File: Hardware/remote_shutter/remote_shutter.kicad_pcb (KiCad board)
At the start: 4 copper layers, 62.5 x 57 mm, 67 parts, among them J1 USB_C_Receptacle_USB2.0, J2 OLED, J3 AudioJack3, J4 Buzzer, J6 Switch, Q1 DMN2056U, Q2 DMN2056U, Q3 BC847BDW1, SW1 RotaryEncoder_Switch, U1 AZ1117-3.3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

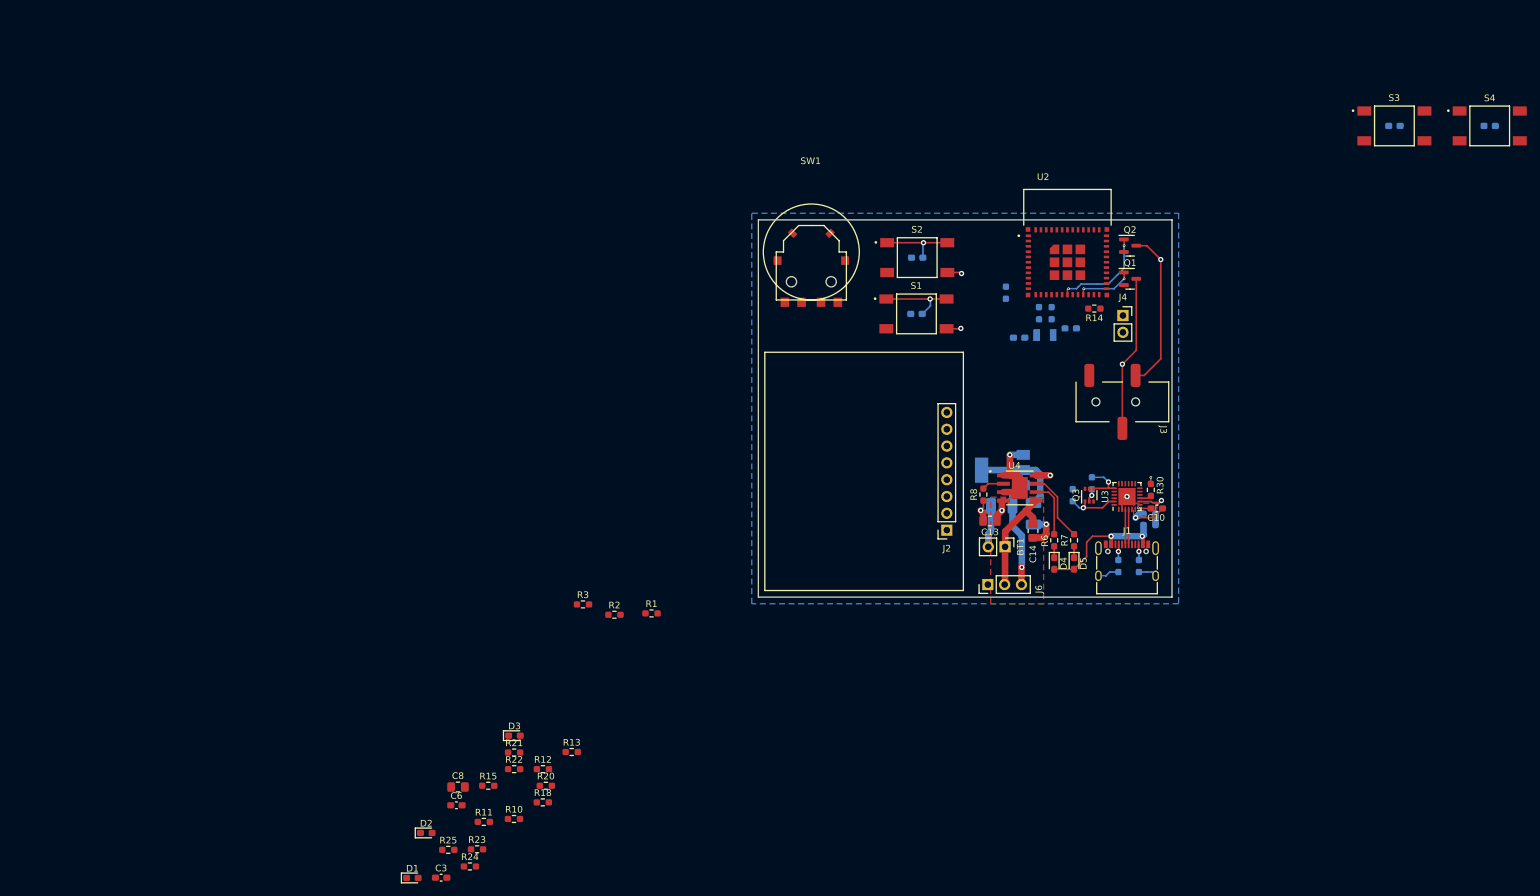
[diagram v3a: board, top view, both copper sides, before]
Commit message: Further routing. Fixed I2C net connection.
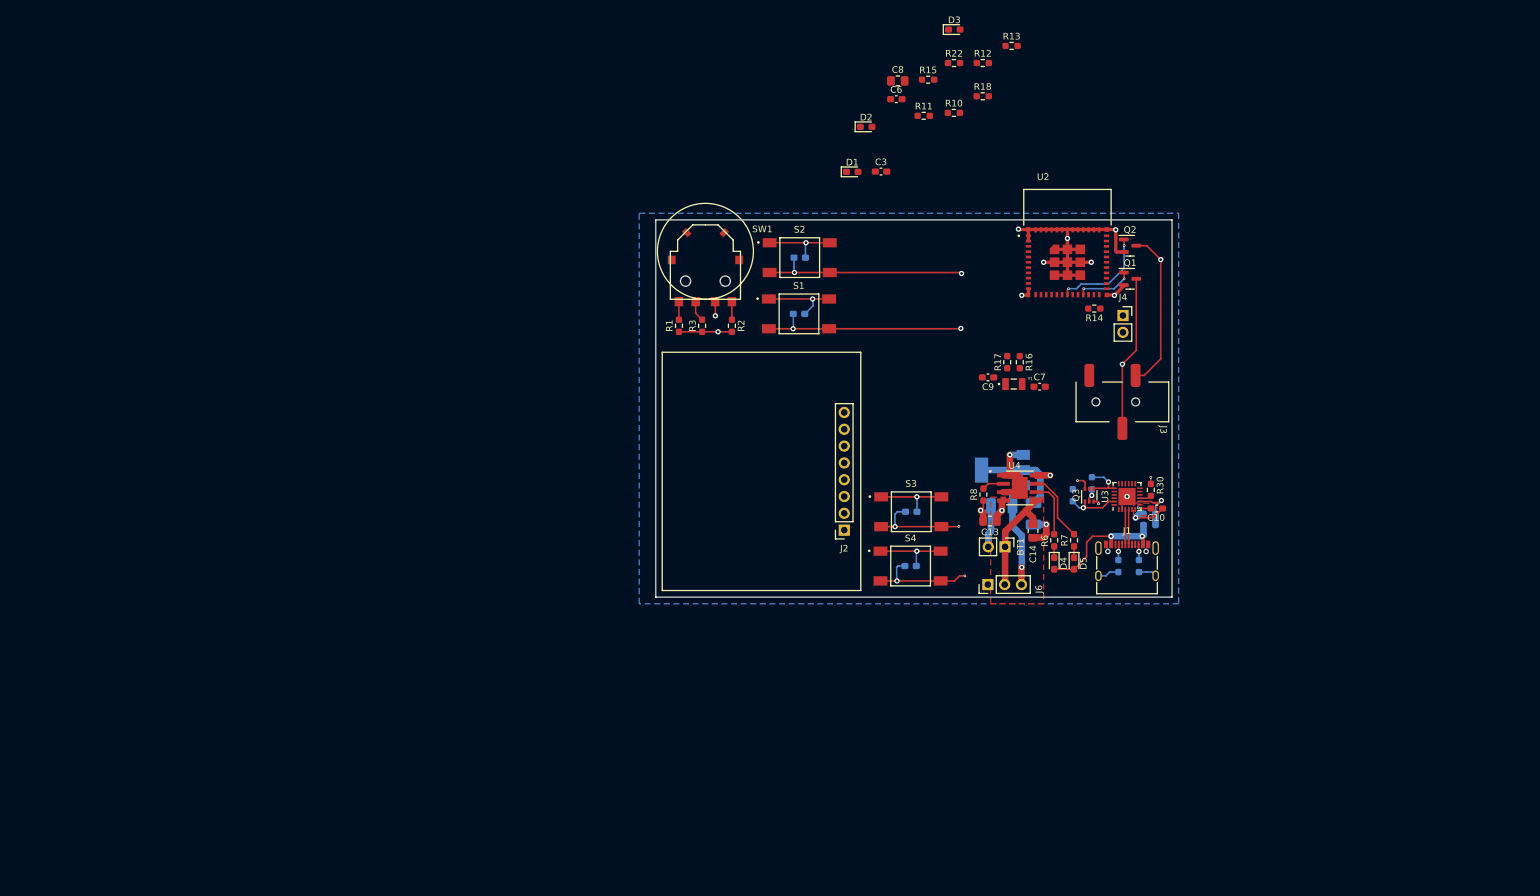
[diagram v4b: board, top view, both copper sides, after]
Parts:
- removed R19, R20, R21, R23, R24, R25: 10k, Resistor_SMD:R_0603_1608Metric_Pad0.98x0.95mm_HandSolder
- C7, C9, R16, R17, Y1: moved to F.Cu
- moved D1 125.7 mm to (170.7, 26.2)
- moved C6 125.7 mm to (177.3, 15.3)
- moved C8 125.7 mm to (177.6, 12.5)
- moved D2 125.7 mm to (172.8, 19.4)
- moved R10 125.7 mm to (186.0, 17.3)
- moved R11 125.7 mm to (181.5, 17.8)
- moved R12 125.7 mm to (190.4, 9.80)
- moved R15 125.7 mm to (182.2, 12.3)
- moved R18 125.7 mm to (190.4, 14.8)
- moved R22 125.7 mm to (186.1, 9.80)
- moved C3 125.7 mm to (175.0, 26.2)
- moved D3 125.7 mm to (186.1, 4.74)
- moved R13 125.7 mm to (194.8, 7.21)
- moved C5 109.9 mm to (179.5, 85.8)
- moved S4 109.9 mm to (179.5, 85.8)
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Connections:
- U2 pad 10: /MCU/B3 -> unconnected-(U2-Pad10)
- U2 pad 16: unconnected-(U2-Pad16) -> /MCU/A3
- U2 pad 27: /MCU/A3 -> unconnected-(U2-Pad27)
- U2 pad 28: /MCU/B3 -> unconnected-(U2-Pad28)
- U2 pad 4: /MCU/C3 -> unconnected-(U2-Pad4)
- U2 pad 9: /MCU/A3 -> unconnected-(U2-Pad9)
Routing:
- net GND: track 67.0 -> 140.0 mm, vias 7 -> 17
- net /MCU/EN: track 0.00 -> 43.2 mm, vias 0 -> 3
- net /MCU/IO0: track 0.00 -> 38.8 mm, vias 0 -> 3
- net /MCU/Interfaces/SHUTTER: track 61.5 -> 90.6 mm, vias 2 -> 3
- net /MCU/Interfaces/FOCUS: track 52.3 -> 81.4 mm, vias 2 -> 3
- net +3V3: track 16.8 -> 24.8 mm, vias 2 -> 3
- net /MCU/Interfaces/A2: track 0.00 -> 3.14 mm
- net /MCU/Interfaces/A1: track 0.00 -> 2.74 mm
- net /MCU/Interfaces/A0: track 0.00 -> 2.74 mm
- net Net-(C7-Pad1): track 0.57 -> 0.00 mm
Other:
- board size 62.5 x 57 mm -> 78 x 57 mm

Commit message: Initial routing complete
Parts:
- moved R18 71.6 mm to (165.3, 81.9)
- moved R22 71.6 mm to (165.3, 78.3)
- moved D3 43.7 mm to (181.1, 48.2)
- moved R15 41.8 mm to (204.0, 48.0), turned to -90 degrees
- moved R12 38.6 mm to (186.1, 48.2)
- moved R13 35.4 mm to (195.2, 42.6), turned to 90 degrees
- moved C8 28.3 mm to (193.2, 36.1), turned to 180 degrees
- moved C6 27.8 mm to (193.4, 38.0), turned to 180 degrees
- moved R11 26.2 mm to (186.1, 43.6)
- moved D2 25.6 mm to (181.1, 43.6)
- moved C3 23.8 mm to (194.4, 40.0), turned to 180 degrees
- moved R10 21.7 mm to (186.1, 39.0)
- moved D1 16.5 mm to (181.1, 39.0)
- moved J4 15.5 mm to (201.5, 59.8)
- moved C9 7.52 mm to (194.2, 50.4)
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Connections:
- J2 pad 1: /MCU/Interfaces/SDA -> /MCU/Interfaces/I2C.SDA
- J2 pad 2: /MCU/Interfaces/SCL -> /MCU/Interfaces/I2C.SCL
- R18 pad 2: /MCU/SDA -> /MCU/Interfaces/I2C.SDA
- R22 pad 2: /MCU/SCL -> /MCU/Interfaces/I2C.SCL
- U2 pad 16: /MCU/A3 -> /MCU/Interfaces/A2
- U2 pad 26: /MCU/SCL -> /MCU/Interfaces/I2C.SCL
- U2 pad 33: /MCU/SDA -> /MCU/Interfaces/I2C.SDA
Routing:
- net /MCU/Interfaces/A0: track 2.74 -> 71.8 mm, vias 0 -> 2
- net /MCU/Interfaces/I2C.SDA: track 0.00 -> 65.5 mm, vias 0 -> 1
- net /MCU/Interfaces/I2C.SCL: track 0.00 -> 60.6 mm, vias 0 -> 1
- net /MCU/Interfaces/A2: track 3.14 -> 61.5 mm, vias 0 -> 2
- net /MCU/EN: track 43.2 -> 93.5 mm, vias 3 -> 4
- net /MCU/Interfaces/A1: track 2.74 -> 52.9 mm, vias 0 -> 2
- net /MCU/RST: track 0.00 -> 47.7 mm, vias 0 -> 1
- net /Comms/RX: track 0.00 -> 38.3 mm, vias 0 -> 2
- net /Comms/TX: track 0.00 -> 38.2 mm, vias 0 -> 2
- net /MCU/IO0: track 38.8 -> 67.9 mm, vias 3 -> 4
- net GND: track 140.0 -> 158.8 mm, vias 17 -> 24
- net Net-(J4-Pad1): track 0.00 -> 15.6 mm
- net Net-(R12-Pad2): track 0.00 -> 15.6 mm, vias 0 -> 2
- net Net-(R11-Pad2): track 0.00 -> 14.0 mm, vias 0 -> 2
- net +3V3: track 24.8 -> 38.0 mm, vias 3 -> 8
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- added copper zone on F.Cu, net (none)
- added copper zone on In1.Cu, net (none)

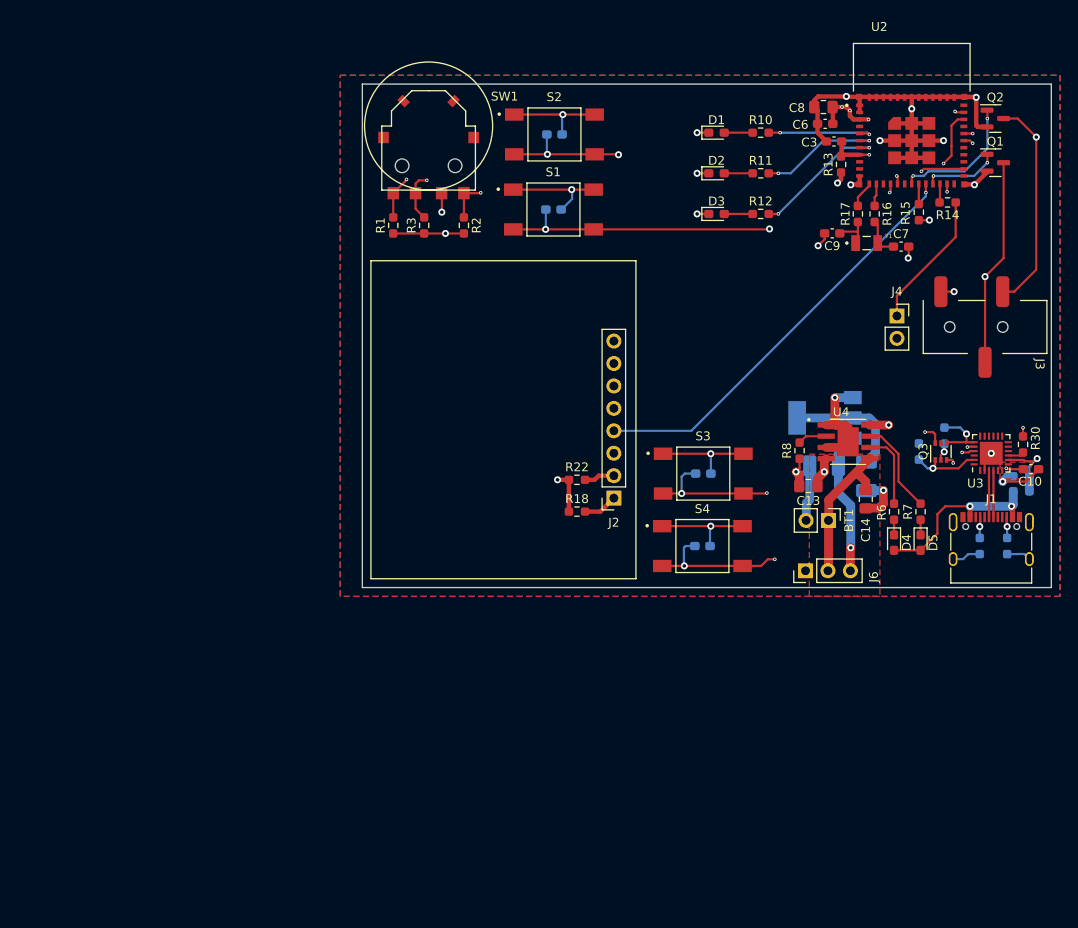
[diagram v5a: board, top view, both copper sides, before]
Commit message: Added logo. Changed RST route.
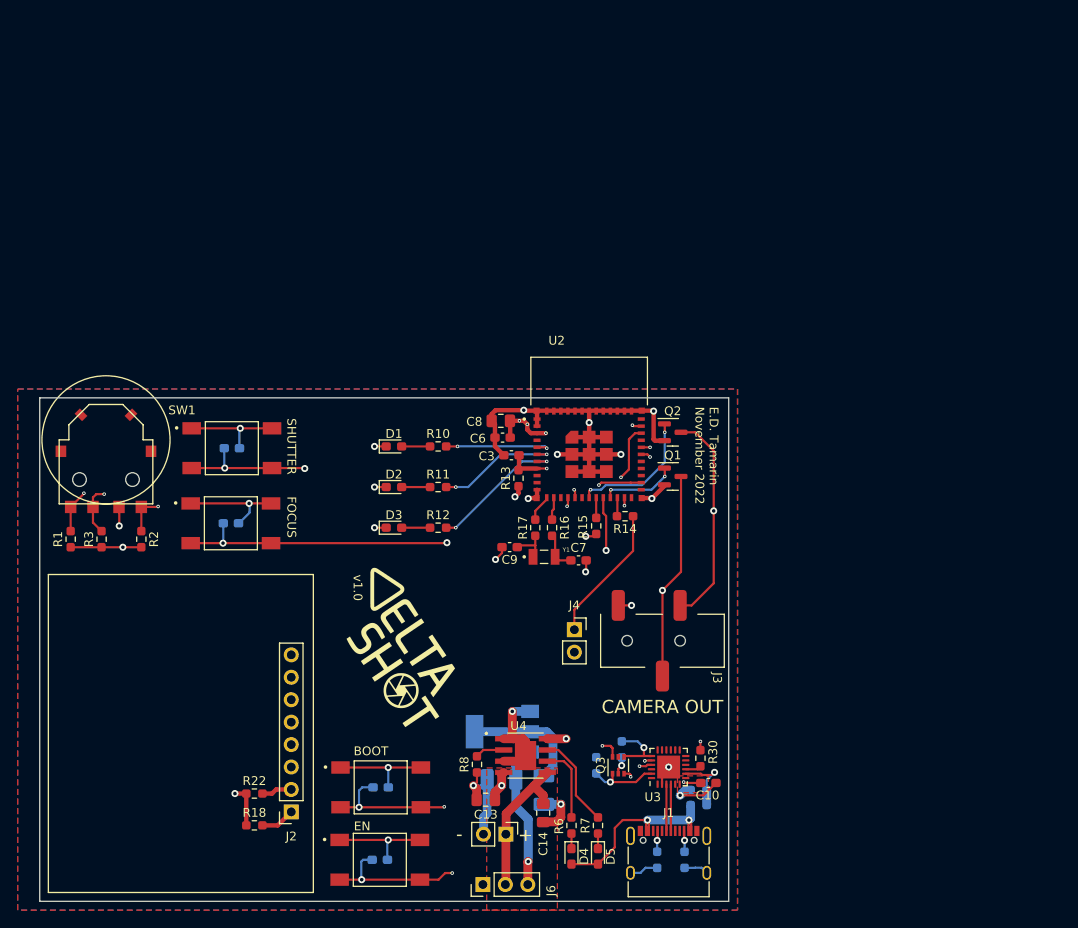
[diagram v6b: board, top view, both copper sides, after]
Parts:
- added G***: LOGO, LOGO, F.Cu at (145.5, 98.0)
- moved C4 50.9 mm to (143.1, 113.1)
- moved C5 50.9 mm to (143.0, 121.3)
- moved J6 50.9 mm to (154.7, 124.1)
- moved Q3 50.9 mm to (170.0, 110.6)
- moved R22 50.9 mm to (128.8, 113.8)
- moved R28 50.9 mm to (179.1, 115.1)
- moved R30 50.9 mm to (179.3, 109.8)
- moved R31 50.9 mm to (170.4, 108.8)
- moved R32 50.9 mm to (167.5, 110.6)
- moved R4 50.9 mm to (177.5, 121.3)
- moved R5 50.9 mm to (174.4, 121.3)
- moved S3 50.9 mm to (143.1, 113.1)
- moved S4 50.9 mm to (143.0, 121.3)
- moved U1 50.9 mm to (156.9, 106.8)
- moved BT1 50.9 mm to (157.3, 118.4)
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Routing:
- net /MCU/RST: track 47.7 -> 51.9 mm
- net /MCU/Interfaces/SHUTTER: track 90.6 -> 87.8 mm
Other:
- board text added: "+"
- board text added: "-"
- board text added: "BOOT"
- board text added: "CAMERA OUT"
- board text added: "E.D. Tamarin November 2022"
- board text added: "EN"
- board text added: "FOCUS"
- board text added: "SHUTTER"
- board text added: "v1.0"

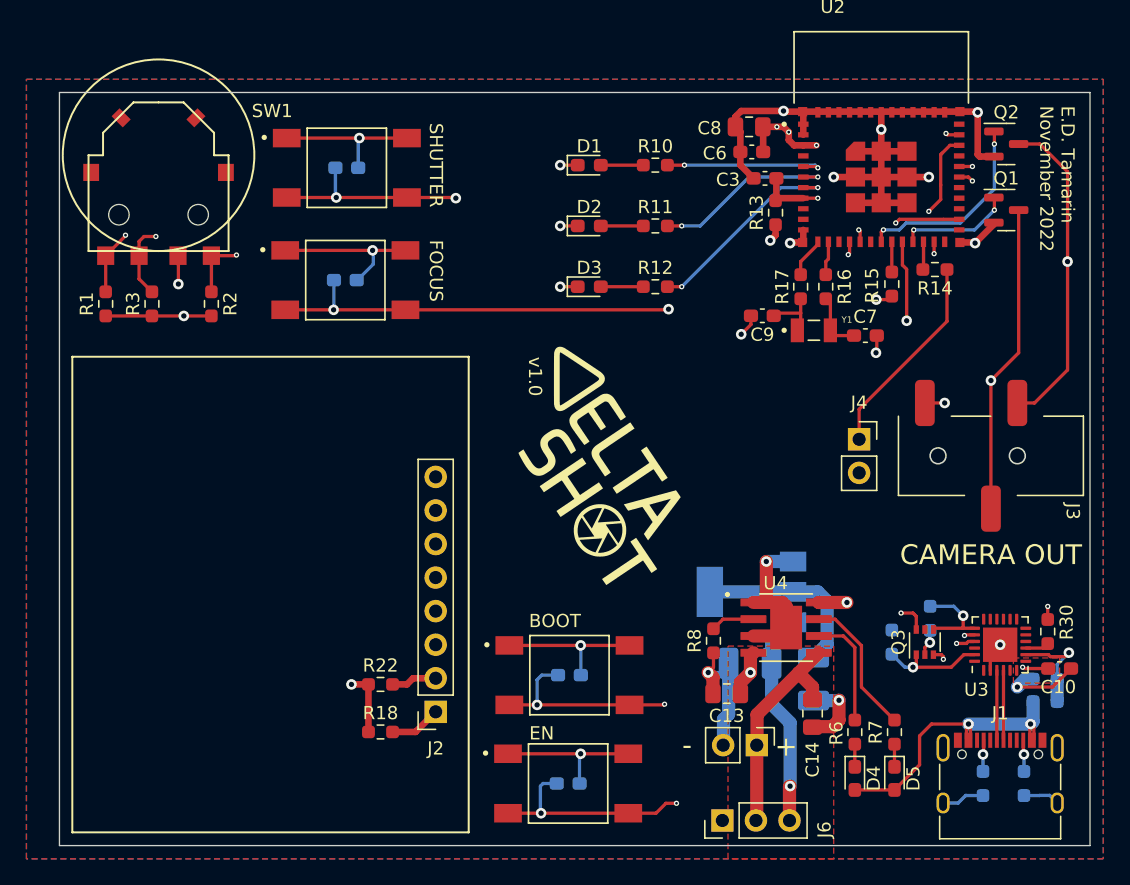
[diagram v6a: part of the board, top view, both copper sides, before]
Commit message: Fixed cap placement
C11 and C12 were placed under the battery
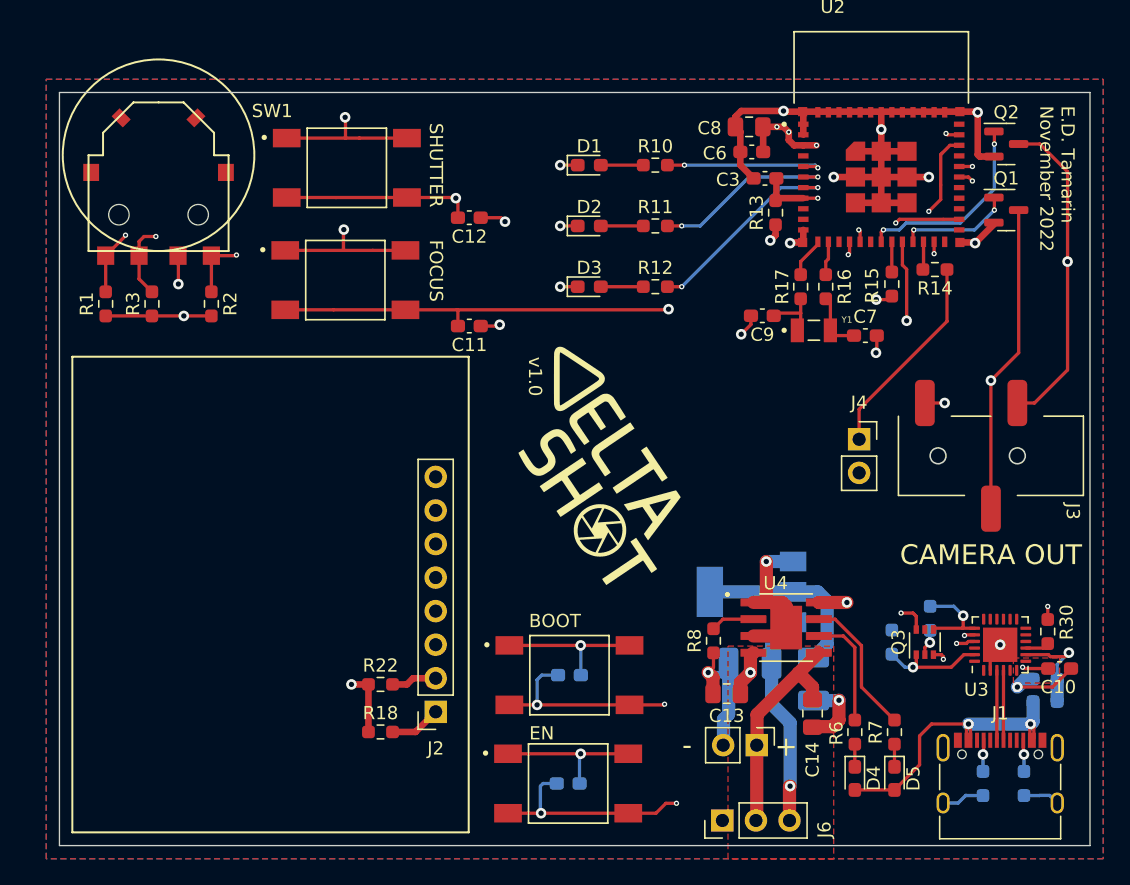
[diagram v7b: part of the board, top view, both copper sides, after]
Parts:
- C11, C12: moved to F.Cu
- moved C12 10.0 mm to (135.5, 78.5)
- moved C11 10.0 mm to (135.5, 86.7)
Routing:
- net GND: track 158.9 -> 160.4 mm, vias 24 -> 26
- net /MCU/Interfaces/FOCUS: track 81.4 -> 80.4 mm, vias 3 -> 2
- net /MCU/Interfaces/SHUTTER: track 87.8 -> 87.1 mm, vias 3 -> 2
